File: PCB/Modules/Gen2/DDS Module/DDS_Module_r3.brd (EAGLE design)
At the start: 55.7 x 77.8 mm, 38 parts, among them IC1 SN65HVD31DR, IC2 LM3480-5.0, IC3 AD9834, IC4 SN65HVD31DR, IC5 AD5620BRJZ-2500RL7, J1 BNCPTH, Y1 ASE10MHZ

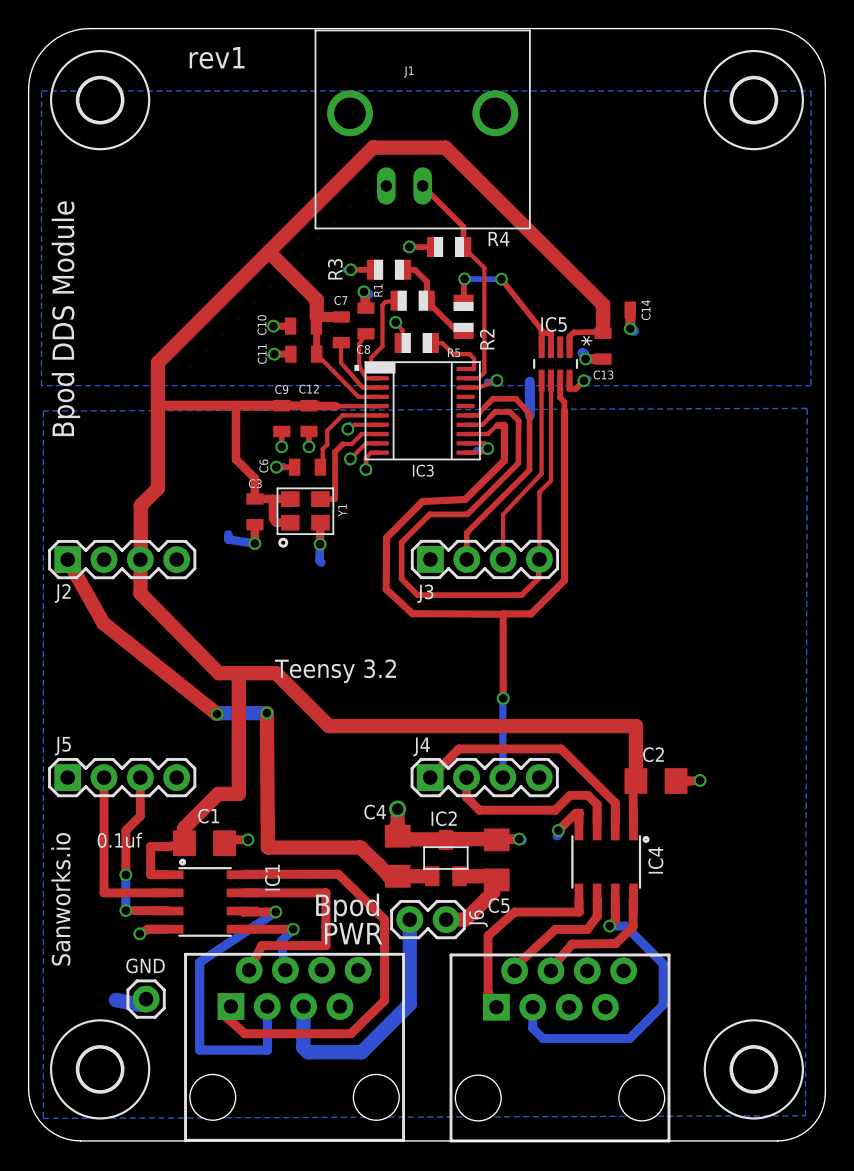
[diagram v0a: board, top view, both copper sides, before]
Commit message: -Critical Update for modules with optional RJ45 power (ValveDriver, I2C, SNES and DDS); new PCB designs add a diode to prevent USB power from entering output pin of 5V regulator, when RJ45 (state machine) power is not connected. This update greatly reduces unnecessary power consumption and heat dissipation. If you built a board using the previous designs, please Email a photo of your board to Sanworks support for a free upgrade. -Updated component names on some boards and on web BOMs to avoid skipping parts -Renamed Gen2 module PCB folder from '0.7' to 'Gen2' -Retired pocket state machine (to be replaced with Bpod State Machine r1)
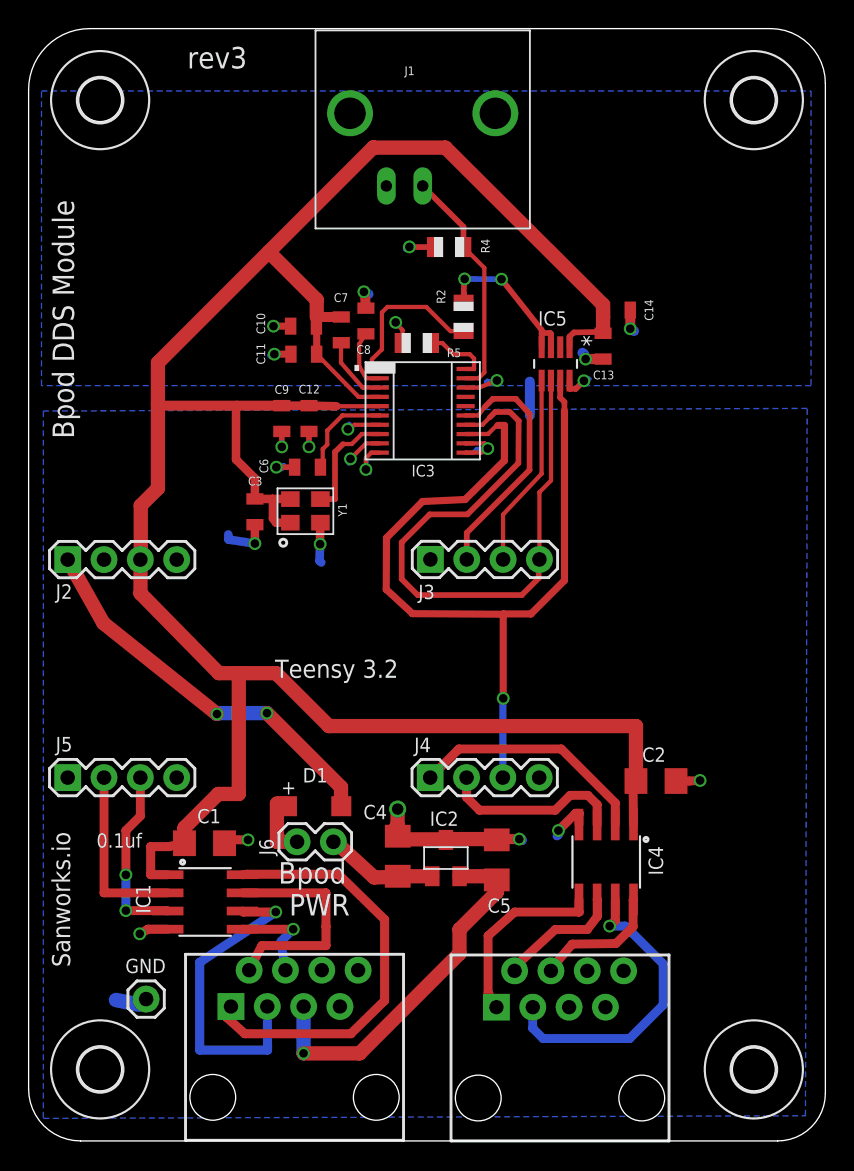
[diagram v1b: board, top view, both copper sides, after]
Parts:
- removed R1: 5.6k, adafruit:R0805
- removed R3: 470, adafruit:R0805
- added D1: MBR0520LT, diode:SOD123
- R2: value 820 -> 6.8k
- moved J6 9.58 mm to (21.6, 20.9)
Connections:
- removed net N$19: R1.1, R2.1, R3.2
- removed net N$26: C5.2, IC2.2, J6.1
- new net N$14: C4.2, IC2.1, J6.1
- new net N$6: IC3.1, R2.1
- net 5V: now also D1.C; no longer C4.2, IC2.1
- net GND: no longer R3.1
- net N$18: now also D1.A, J6.2; no longer IC3.1, R1.2
- net N$24: now also C5.2, IC2.2; no longer J6.2
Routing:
- net 5V: track 41.1 -> 27.5 mm
- net N$6: track 0.00 -> 11.3 mm
- net N$24: track 17.7 -> 26.0 mm, vias 0 -> 1
- net N$14: track 0.00 -> 7.87 mm
- net N$26: track 7.75 -> 0.00 mm
- net N$19: track 6.78 -> 0.00 mm
- net GND: track 66.9 -> 64.8 mm, vias 25 -> 24
- net N$18: track 6.62 -> 4.95 mm
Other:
- board text added: "+"
- board text added: "rev3"
- board text removed: "rev1"
